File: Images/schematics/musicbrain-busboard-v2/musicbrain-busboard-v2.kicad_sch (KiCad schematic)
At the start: 84 parts, among them J1 SLOT 1, J10 EXP, J11 DISPLAY, J12 QWIIC, J13 MIDI IN1, J14 MIDI IN2, J15 MIDI OUT, J16 CAN, J17 AUDIO/CODEC, J18 TUNE, J19 DLG1 (Serial3), J2 SLOT 2, J20 DLG2 (Serial4), J21 EXPANSION, J3 SLOT 3, J4 SLOT 4, J5 SLOT 5, J6 SLOT 6, J7 HUB 1, J8 HUB 2, J9 PWR IN, U1 Teensy 4.1, U10 H11L1, U11 74LVC1G17, U12 SN65HVD230, U13 74LVC1G17, U2 R-78E5.0-0.5, U3 AMS1117-3.3, U4 74HC154, U5 74HC165, U6 74HC165, U7 74LVC1G125, U8 74LVC245, U9 H11L1

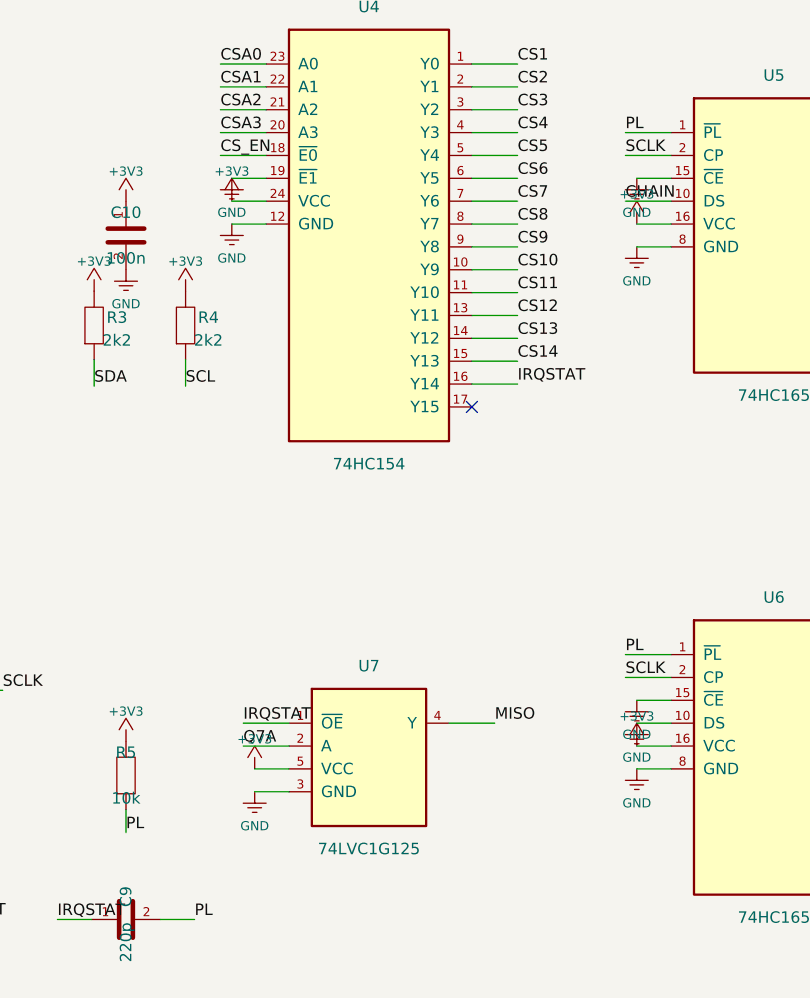
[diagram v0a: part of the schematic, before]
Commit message: Busboard v2: ontkoppel-C's voor U5/U6/buffers (C15-C17)
Co-Authored-By: Claude Fable 5 <noreply@anthropic.com>
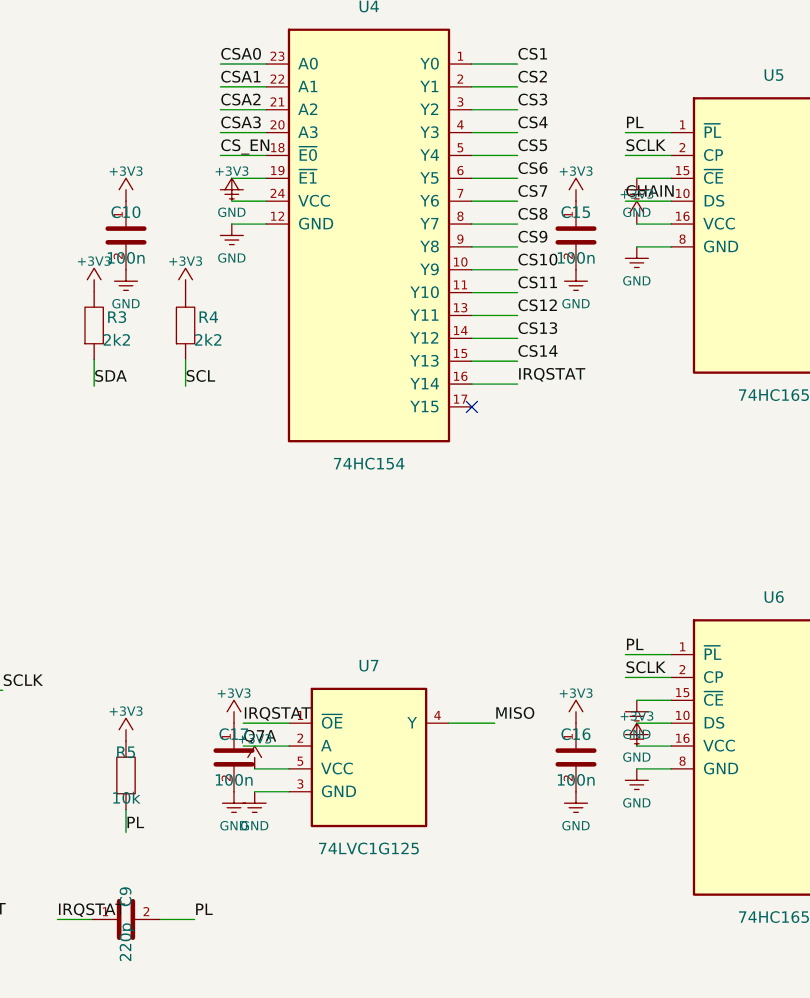
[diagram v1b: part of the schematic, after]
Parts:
- removed D1, D2: 1N4148WS, Diode_SMD:D_SOD-323, symbol Device:D
- removed J16: CAN, Connector_PinHeader_2.54mm:PinHeader_1x04_P2.54mm_Vertical, symbol Custom:Conn_01x04
- removed J19: DLG1 (Serial3), Connector_PinHeader_2.54mm:PinHeader_1x04_P2.54mm_Vertical, symbol Custom:Conn_01x04
- removed R14: 100k, Resistor_SMD:R_0805_2012Metric, symbol Device:R
- added C12, C16, C17: 100n, Capacitor_SMD:C_0805_2012Metric, symbol Device:C
- added D3: BAT54S, Package_TO_SOT_SMD:SOT-23, symbol Custom:BAT54S
- added J14: MIDI IN2, Connector_PinHeader_2.54mm:PinHeader_1x03_P2.54mm_Vertical, symbol Custom:Conn_01x03
- added J17: AUDIO/CODEC, Connector_PinHeader_2.54mm:PinHeader_2x07_P2.54mm_Vertical, symbol Custom:Conn_02x07
- added J18: TUNE, Connector_PinHeader_2.54mm:PinHeader_1x02_P2.54mm_Vertical, symbol Custom:Conn_01x02
- added R21: 100k, Resistor_SMD:R_0805_2012Metric, symbol Device:R
- C15: renamed from C9; value 220p -> 100n
- C9: renamed from R21; value 100k -> 220p; footprint Resistor_SMD:R_0805_2012Metric -> Capacitor_SMD:C_0805_2012Metric; symbol Device:R -> Device:C
- D1: renamed from J14; value MIDI IN2 -> 1N4148WS; footprint Connector_PinHeader_2.54mm:PinHeader_1x03_P2.54mm_Vertical -> Diode_SMD:D_SOD-323; symbol Custom:Conn_01x03 -> Device:D
- D2: renamed from C12; value 100n -> 1N4148WS; footprint Capacitor_SMD:C_0805_2012Metric -> Diode_SMD:D_SOD-323; symbol Device:C -> Device:D
- J16: renamed from J18; value TUNE -> CAN; footprint Connector_PinHeader_2.54mm:PinHeader_1x02_P2.54mm_Vertical -> Connector_PinHeader_2.54mm:PinHeader_1x04_P2.54mm_Vertical; symbol Custom:Conn_01x02 -> Custom:Conn_01x04
- J19: renamed from J20; value DLG2 (Serial4) -> DLG1 (Serial3)
- J20: renamed from J17; value AUDIO/CODEC -> DLG2 (Serial4); footprint Connector_PinHeader_2.54mm:PinHeader_2x07_P2.54mm_Vertical -> Connector_PinHeader_2.54mm:PinHeader_1x04_P2.54mm_Vertical; symbol Custom:Conn_02x07 -> Custom:Conn_01x04
- R14: renamed from D3; value BAT54S -> 100k; footprint Package_TO_SOT_SMD:SOT-23 -> Resistor_SMD:R_0805_2012Metric; symbol Custom:BAT54S -> Device:R
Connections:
- net +12V: now also J16.4 (Pin_4), J17.1 (Pin_1); no longer J20.1 (Pin_1)
- net +3V3: now also C15.1, C12.1, C16.1, C17.1, D3.2 (K2), J17.5 (Pin_5); no longer D2.1, J20.5 (Pin_5), R14.2 (K2)
- net +5V: now also J17.4 (Pin_4); no longer J20.4 (Pin_4)
- net -12V: now also J17.2 (Pin_2); no longer J20.2 (Pin_2)
- net BCLK1: now also J17.8 (Pin_8); no longer J20.8 (Pin_8)
- net CANH: now also J16.1 (Pin_1)
- net CANL: now also J16.2 (Pin_2)
- net CODEC_RST: now also J17.12 (Pin_12); no longer J20.12 (Pin_12)
- net DLG1_RX: now also J19.3 (Pin_3)
- net DLG1_TX: now also J19.2 (Pin_2)
- net DLG2_RX: now also J20.3 (Pin_3); no longer J19.3 (Pin_3)
- net DLG2_TX: now also J20.2 (Pin_2); no longer J19.2 (Pin_2)
- net GND: now also C15.2, J16.3 (Pin_3), J20.1 (Pin_1), J20.4 (Pin_4), C12.2, C16.2, C17.2, D3.1 (A1), J17.3 (Pin_3), J17.6 (Pin_6), J18.2 (Pin_2), R21.2; no longer C9.2, D2.2, J16.2 (Pin_2), J20.3 (Pin_3), J20.6 (Pin_6), R14.1 (A1)
- net I2S_IN: now also J17.11 (Pin_11); no longer J20.11 (Pin_11)
- net I2S_OUT: now also J17.10 (Pin_10); no longer J20.10 (Pin_10)
- net IRQ1: now also R21.1; no longer C9.1
- net IRQSTAT: now also C9.1; no longer C15.1
- net LRCLK1: now also J17.9 (Pin_9); no longer J20.9 (Pin_9)
- net MCLK1: now also J17.7 (Pin_7); no longer J20.7 (Pin_7)
- net MIN1_5: now also D1.2 (A)
- net MIN1_A: now also D1.1 (K)
- net MIN2_4: now also J14.1 (Pin_1); no longer D1.1 (Pin_1)
- net MIN2_5: now also D2.2 (A), J14.2 (Pin_2); no longer D1.2 (Pin_2)
- net MIN2_A: now also D2.1 (K)
- net PL: now also C9.2; no longer C15.2
- net SCL: now also J17.14 (Pin_14); no longer J20.14 (Pin_14)
- net SDA: now also J17.13 (Pin_13); no longer J20.13 (Pin_13)
- net TUNE_J: now also R14.1, J18.1 (Pin_1); no longer J16.1 (Pin_1)
- net TUNE_N: now also R14.2, D3.3 (K1A2); no longer R14.3 (K1A2)
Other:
- moved on the sheet: C15, J19

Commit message: Busboard v2: schema-iteraties (geometrie-gedreven pinvolgordes) + PCB-router in aanbouw
Schema (ERC 0, netlijst OK): J16/J17/J21-pinvolgordes geometrie-gedreven
herordend, U5-D-ingangen geremapt naar de bordgeometrie (noordrij = IRQ1-4;
fw-bitvolgorde gedocumenteerd in het schema), 2e PL-RC (PL2) lokaal bij U6,
codec-I2C via de Qwiic-keten. PCB-generator: volledige placement + netcheck
GROEN (alle pads dragen het juiste net) + lanes/slot-taps/hub-waaiers/display
uit v1 bewezen hergebruikt; nieuwe clusters geroute, NW-kwadrant-detailroutes
nog in DRC-iteratie (~800 -> doel 0). Bordbestand bewust NIET gecommit
(werkregel: alleen DRC 0/0).

Co-Authored-By: Claude Fable 5 <noreply@anthropic.com>
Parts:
- removed D1, D2: 1N4148WS, Diode_SMD:D_SOD-323, symbol Device:D
- removed J16: CAN, Connector_PinHeader_2.54mm:PinHeader_1x04_P2.54mm_Vertical, symbol Custom:Conn_01x04
- removed J19: DLG1 (Serial3), Connector_PinHeader_2.54mm:PinHeader_1x04_P2.54mm_Vertical, symbol Custom:Conn_01x04
- removed R14: 100k, Resistor_SMD:R_0805_2012Metric, symbol Device:R
- added C12: 100n, Capacitor_SMD:C_0805_2012Metric, symbol Device:C
- added D3: BAT54S, Package_TO_SOT_SMD:SOT-23, symbol Custom:BAT54S
- added J14: MIDI IN2, Connector_PinHeader_2.54mm:PinHeader_1x03_P2.54mm_Vertical, symbol Custom:Conn_01x03
- added J17: AUDIO/CODEC, Connector_PinHeader_2.54mm:PinHeader_2x07_P2.54mm_Vertical, symbol Custom:Conn_02x07
- added J18: TUNE, Connector_PinHeader_2.54mm:PinHeader_1x02_P2.54mm_Vertical, symbol Custom:Conn_01x02
- added R21: 100k, Resistor_SMD:R_0805_2012Metric, symbol Device:R
- added R33: 10k, Resistor_SMD:R_0805_2012Metric, symbol Device:R
- C18: renamed from R21; value 100k -> 220p; footprint Resistor_SMD:R_0805_2012Metric -> Capacitor_SMD:C_0805_2012Metric; symbol Device:R -> Device:C
- D1: renamed from J14; value MIDI IN2 -> 1N4148WS; footprint Connector_PinHeader_2.54mm:PinHeader_1x03_P2.54mm_Vertical -> Diode_SMD:D_SOD-323; symbol Custom:Conn_01x03 -> Device:D
- D2: renamed from C12; value 100n -> 1N4148WS; footprint Capacitor_SMD:C_0805_2012Metric -> Diode_SMD:D_SOD-323; symbol Device:C -> Device:D
- J16: renamed from J18; value TUNE -> CAN; footprint Connector_PinHeader_2.54mm:PinHeader_1x02_P2.54mm_Vertical -> Connector_PinHeader_2.54mm:PinHeader_1x04_P2.54mm_Vertical; symbol Custom:Conn_01x02 -> Custom:Conn_01x04
- J19: renamed from J20; value DLG2 (Serial4) -> DLG1 (Serial3)
- J20: renamed from J17; value AUDIO/CODEC -> DLG2 (Serial4); footprint Connector_PinHeader_2.54mm:PinHeader_2x07_P2.54mm_Vertical -> Connector_PinHeader_2.54mm:PinHeader_1x04_P2.54mm_Vertical; symbol Custom:Conn_02x07 -> Custom:Conn_01x04
- R14: renamed from D3; value BAT54S -> 100k; footprint Package_TO_SOT_SMD:SOT-23 -> Resistor_SMD:R_0805_2012Metric; symbol Custom:BAT54S -> Device:R
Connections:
- net +12V: now also J16.1 (Pin_1), J17.11 (Pin_11); no longer J20.1 (Pin_1)
- net +3V3: now also C12.1, D3.2 (K2), J17.1 (Pin_1), R33.1; no longer D2.1, J20.5 (Pin_5), R14.2 (K2)
- net +5V: now also J17.3 (Pin_3); no longer J20.4 (Pin_4)
- net -12V: now also J17.13 (Pin_13); no longer J20.2 (Pin_2)
- net BCLK1: now also J17.6 (Pin_6); no longer J20.8 (Pin_8)
- net CANH: now also J16.2 (Pin_2)
- net CANL: now also J16.3 (Pin_3)
- net CODEC_RST: now also U1.44 (22), J17.2 (Pin_2); no longer J20.12 (Pin_12), U1.25 (33)
- net CS10: now also J21.3 (Pin_3); no longer J21.12 (Pin_12)
- net CS11: now also J21.5 (Pin_5); no longer J21.13 (Pin_13)
- net CS12: now also J21.7 (Pin_7); no longer J21.14 (Pin_14)
- net CS13: now also J21.9 (Pin_9); no longer J21.15 (Pin_15)
- net CS14: now also J21.11 (Pin_11); no longer J21.16 (Pin_16)
- net CS9: now also J21.1 (Pin_1); no longer J21.11 (Pin_11)
- net DLG1_RX: now also J19.3 (Pin_3)
- net DLG1_TX: now also J19.2 (Pin_2)
- net DLG2_RX: now also J20.3 (Pin_3); no longer J19.3 (Pin_3)
- net DLG2_TX: now also J20.2 (Pin_2); no longer J19.2 (Pin_2)
- net GND: now also J16.4 (Pin_4), J20.1 (Pin_1), J20.4 (Pin_4), J21.14 (Pin_14), J21.16 (Pin_16), J21.18 (Pin_18), J21.20 (Pin_20), J21.25 (Pin_25), J21.26 (Pin_26), U5.3 (D4), U5.4 (D5), C12.2, D3.1 (A1), J17.14 (Pin_14), J17.5 (Pin_5), J17.7 (Pin_7), J17.9 (Pin_9), J18.2 (Pin_2), R21.2; no longer C18.2, D2.2, J16.2 (Pin_2), J20.3 (Pin_3), J20.6 (Pin_6), J21.1 (Pin_1), J21.10 (Pin_10), J21.17 (Pin_17), J21.24 (Pin_24), J21.3 (Pin_3), J21.6 (Pin_6), R14.1 (A1), U5.11 (D0), U5.12 (D1)
- net I2S_IN: now also J17.12 (Pin_12); no longer J20.11 (Pin_11)
- net I2S_OUT: now also J17.10 (Pin_10); no longer J20.10 (Pin_10)
- net IRQ1: now also U5.14 (D3), R21.1; no longer C18.1, U5.6 (D7)
- net IRQ10: now also J21.8 (Pin_8); no longer J21.21 (Pin_21)
- net IRQ11: now also J21.10 (Pin_10); no longer J21.22 (Pin_22)
- net IRQ12: now also J21.12 (Pin_12); no longer J21.23 (Pin_23)
- net IRQ2: now also U5.13 (D2); no longer U5.5 (D6)
- net IRQ3: now also U5.12 (D1); no longer U5.4 (D5)
- net IRQ4: now also U5.11 (D0); no longer U5.3 (D4)
- net IRQ5: now also U5.6 (D7); no longer U5.14 (D3)
- net IRQ6: now also U5.5 (D6); no longer U5.13 (D2)
- net IRQ7: now also J21.2 (Pin_2); no longer J21.18 (Pin_18)
- net IRQ8: now also J21.4 (Pin_4); no longer J21.19 (Pin_19)
- net IRQ9: now also J21.6 (Pin_6); no longer J21.20 (Pin_20)
- net IRQSTAT: now also C18.1
- net LRCLK1: now also J17.8 (Pin_8); no longer J20.9 (Pin_9)
- net MCLK1: now also J17.4 (Pin_4); no longer J20.7 (Pin_7)
- net MIN1_5: now also D1.2 (A)
- net MIN1_A: now also D1.1 (K)
- net MIN2_4: now also J14.1 (Pin_1); no longer D1.1 (Pin_1)
- net MIN2_5: now also D2.2 (A), J14.2 (Pin_2); no longer D1.2 (Pin_2)
- net MIN2_A: now also D2.1 (K)
- net MISO: now also J21.13 (Pin_13); no longer J21.5 (Pin_5)
- net PL: no longer U6.1 (~{PL})
- net SCL: now also J21.24 (Pin_24); no longer J20.14 (Pin_14), J21.26 (Pin_26)
- net SDA: now also J21.22 (Pin_22); no longer J20.13 (Pin_13), J21.25 (Pin_25)
- net TUNE_J: now also R14.1, J18.1 (Pin_1); no longer J16.1 (Pin_1)
- net TUNE_N: now also R14.2, D3.3 (K1A2); no longer R14.3 (K1A2)
- net XCONVST: now also J21.21 (Pin_21); no longer J21.8 (Pin_8)
- net XLDAC: now also J21.19 (Pin_19); no longer J21.7 (Pin_7)
- net XMOSI: now also J21.17 (Pin_17); no longer J21.4 (Pin_4)
- net XRST: now also J21.23 (Pin_23); no longer J21.9 (Pin_9)
- net XSCLK: now also J21.15 (Pin_15); no longer J21.2 (Pin_2)
- net D22 renamed D33
- net D33: now also U1.25 (33); no longer U1.44 (22)
- new net PL2: C18.2, R33.2, U6.1 (~{PL})
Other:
- moved on the sheet: J19
